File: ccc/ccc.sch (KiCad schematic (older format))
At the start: 28 parts, among them J1 Conn_02x03_Odd_Even, J2 Conn_01x06_Male, J3 Conn_01x03_Male, Q1 Q_NPN_BCE, Q2 Q_NPN_BCE, SW1 RESET, U1 rt9013-33, U2 LTC3225-1, U4 ESP32-WROOM-32

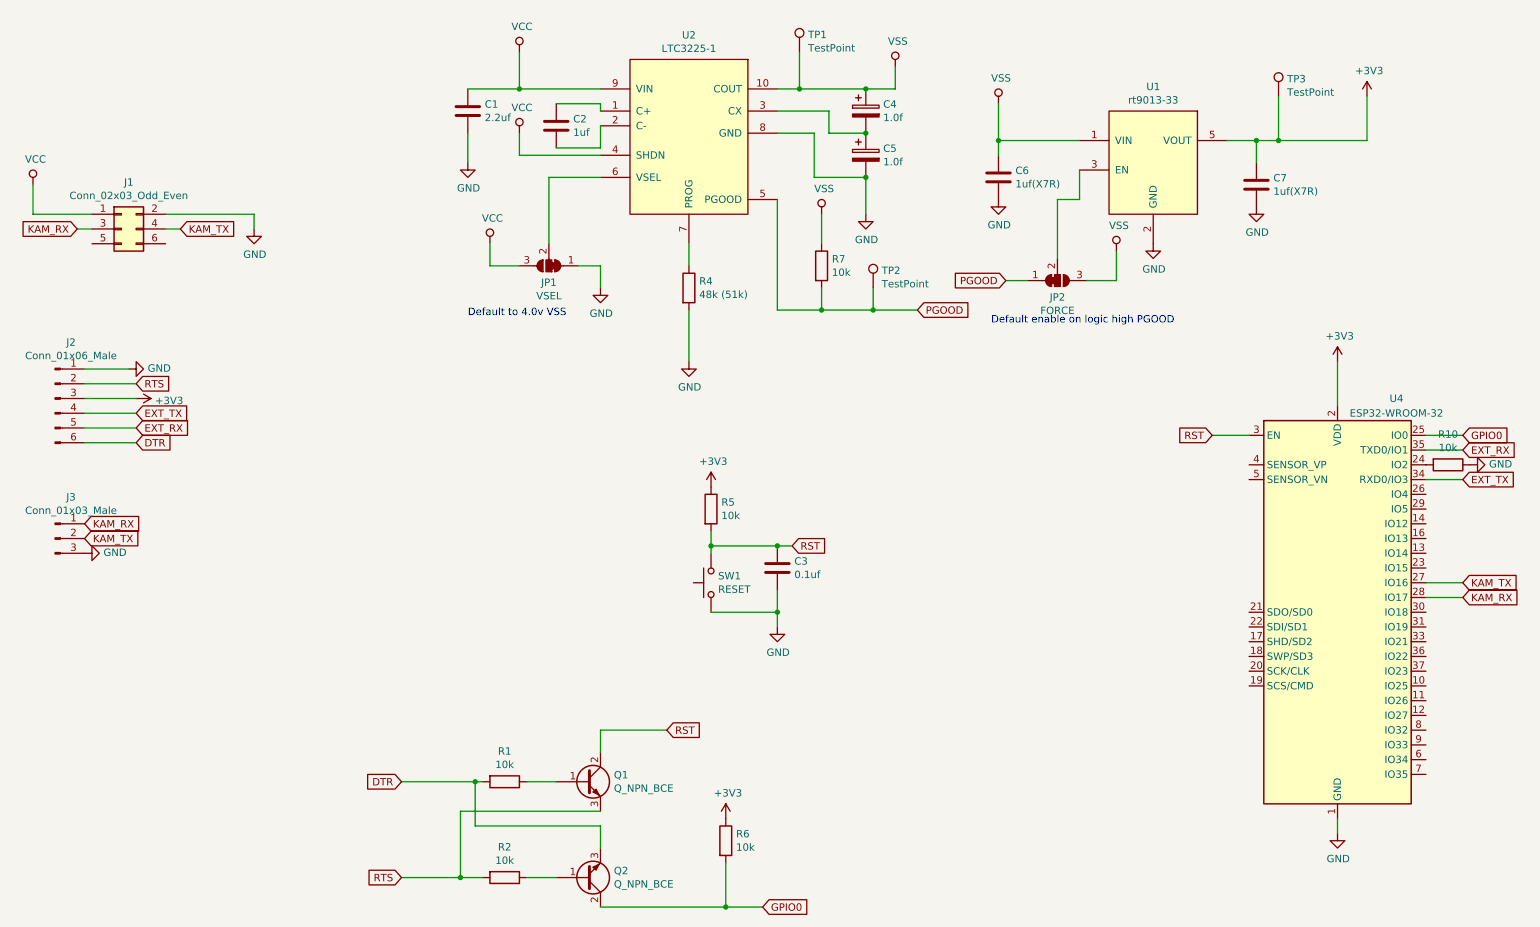
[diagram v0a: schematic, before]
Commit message: Added flipflop - did some layout
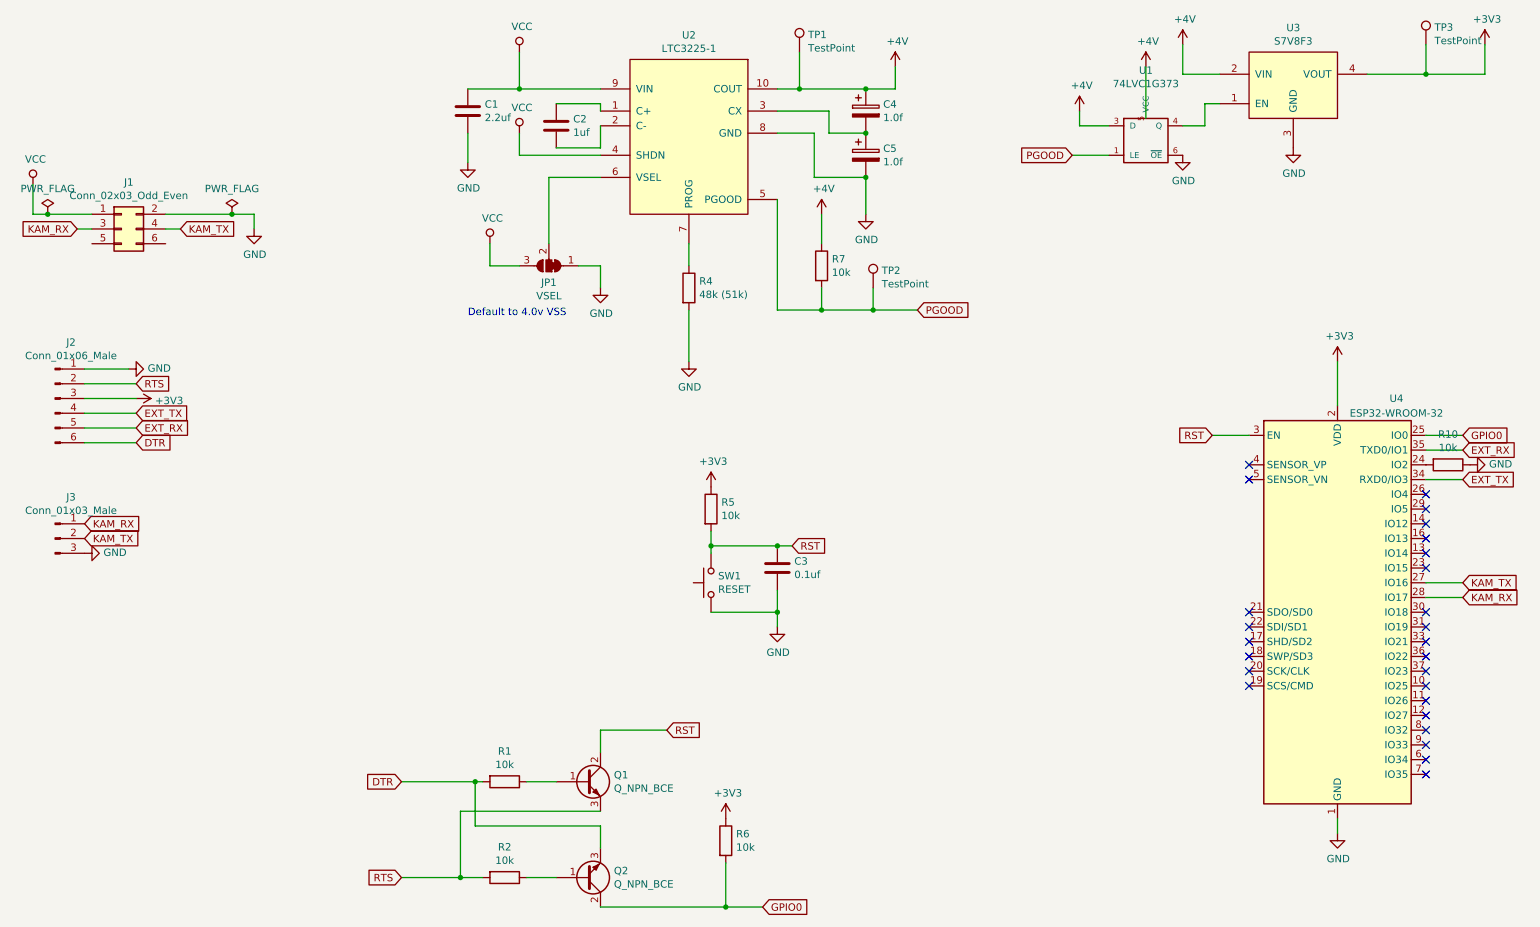
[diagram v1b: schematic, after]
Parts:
- removed C6, C7: 1uf(X7R), Capacitor_SMD:C_1206_3216Metric_Pad1.42x1.75mm_HandSolder, symbol Device:C
- removed JP2: FORCE, Jumper:SolderJumper-3_P1.3mm_Bridged12_RoundedPad1.0x1.5mm, symbol Jumper:SolderJumper_3_Bridged12
- removed U1: rt9013-33, Package_TO_SOT_SMD:SOT-23-5, symbol New_Library:rt9013-33
- added U1: 74LVC1G373, Package_TO_SOT_SMD:SOT-23-6_Handsoldering, symbol New_Library:74LVC1G373
- added U3: S7V8F3, Connector_PinHeader_2.54mm:PinHeader_1x04_P2.54mm_Vertical, symbol New_Library:S7V8F3
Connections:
- net +3V3: now also U3.4 (VOUT)
- net GND: now also U1.2 (GND), U1.6 (~OE), U3.3 (GND)
- net PGOOD: now also U1.1 (LE)
- net VSS renamed +4V
- net +4V: now also U1.3 (D), U1.5 (VCC), U3.2 (VIN)
- new net: U1.4 (Q), U3.1 (EN)
- no-connect marks 0 -> 26
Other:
- note removed: "Default enable on logic high PGOOD"
- moved on the sheet: TP3

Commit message: Fully wired - needs some finish here and there
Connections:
- no-connect marks 26 -> 28
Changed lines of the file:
@@
 Wire Wire Line
 	8700 1050 8700 1400
+NoConn ~ 2050 2250
+NoConn ~ 1550 2250
 $EndSCHEMATC
